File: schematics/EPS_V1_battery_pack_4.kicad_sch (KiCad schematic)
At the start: 31 parts, among them U12 MP2672AGD-0000-Z, U13 MAX17205G+

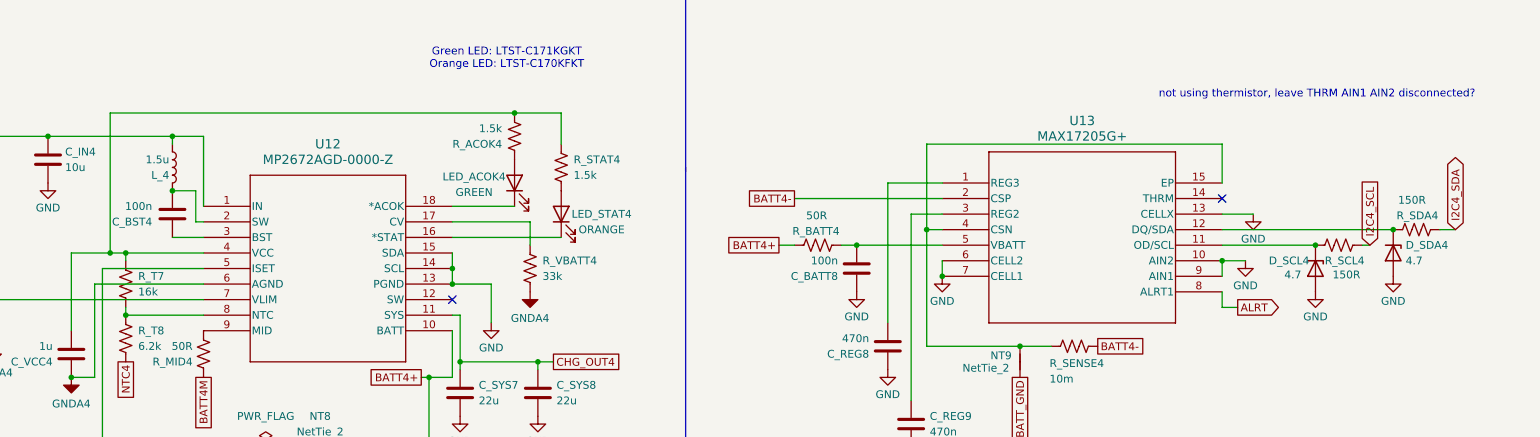
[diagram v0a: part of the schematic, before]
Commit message: Switch out MP28167 for LTC3119 (MPPC buck-boost) in schematic
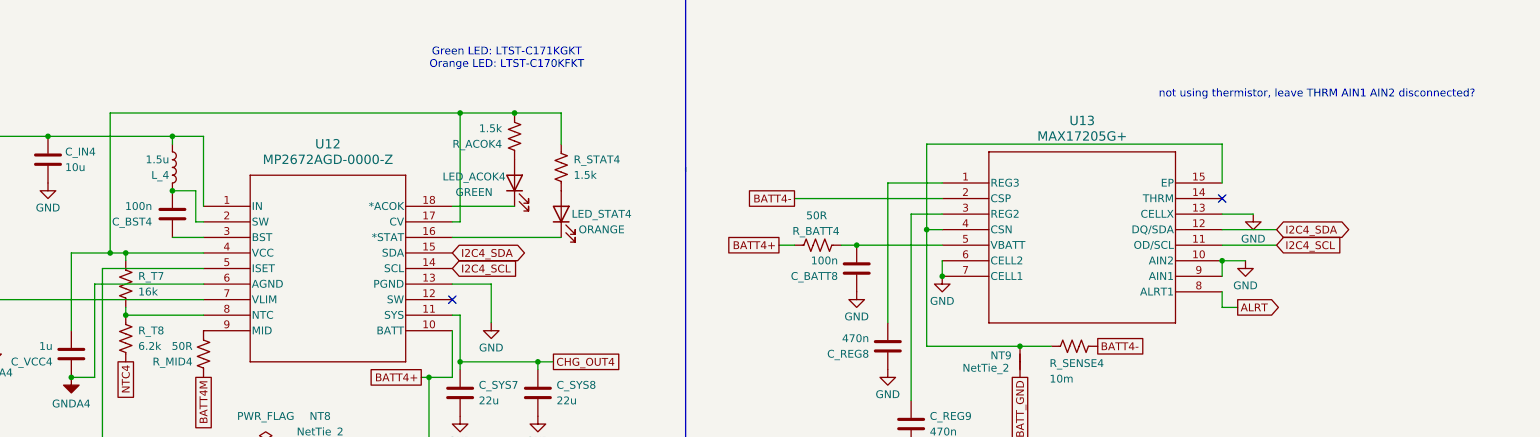
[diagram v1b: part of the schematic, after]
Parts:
- removed D_SCL4, D_SDA4: 4.7, Diode_SMD:D_0603_1608Metric, symbol Device:D_Zener
- removed R_SCL4, R_SDA4: 150R, Resistor_SMD:R_0603_1608Metric, symbol Device:R_US
- removed R_VBATT4: 33k, Resistor_SMD:R_0603_1608Metric, symbol Device:R_US
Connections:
- net GND: no longer U12.14 (SCL), U12.15 (SDA)
- net I2C4_SCL: now also U12.14 (SCL), U13.11 (OD/SCL)
- net I2C4_SDA: now also U12.15 (SDA), U13.12 (DQ/SDA)
- net at C_VCC4.2, R_ACOK4.2, R_STAT4.1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: now also U12.17 (CV)
